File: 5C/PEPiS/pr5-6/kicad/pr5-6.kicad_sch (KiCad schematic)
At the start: 10 parts, among them U1 STM32F103C8T6

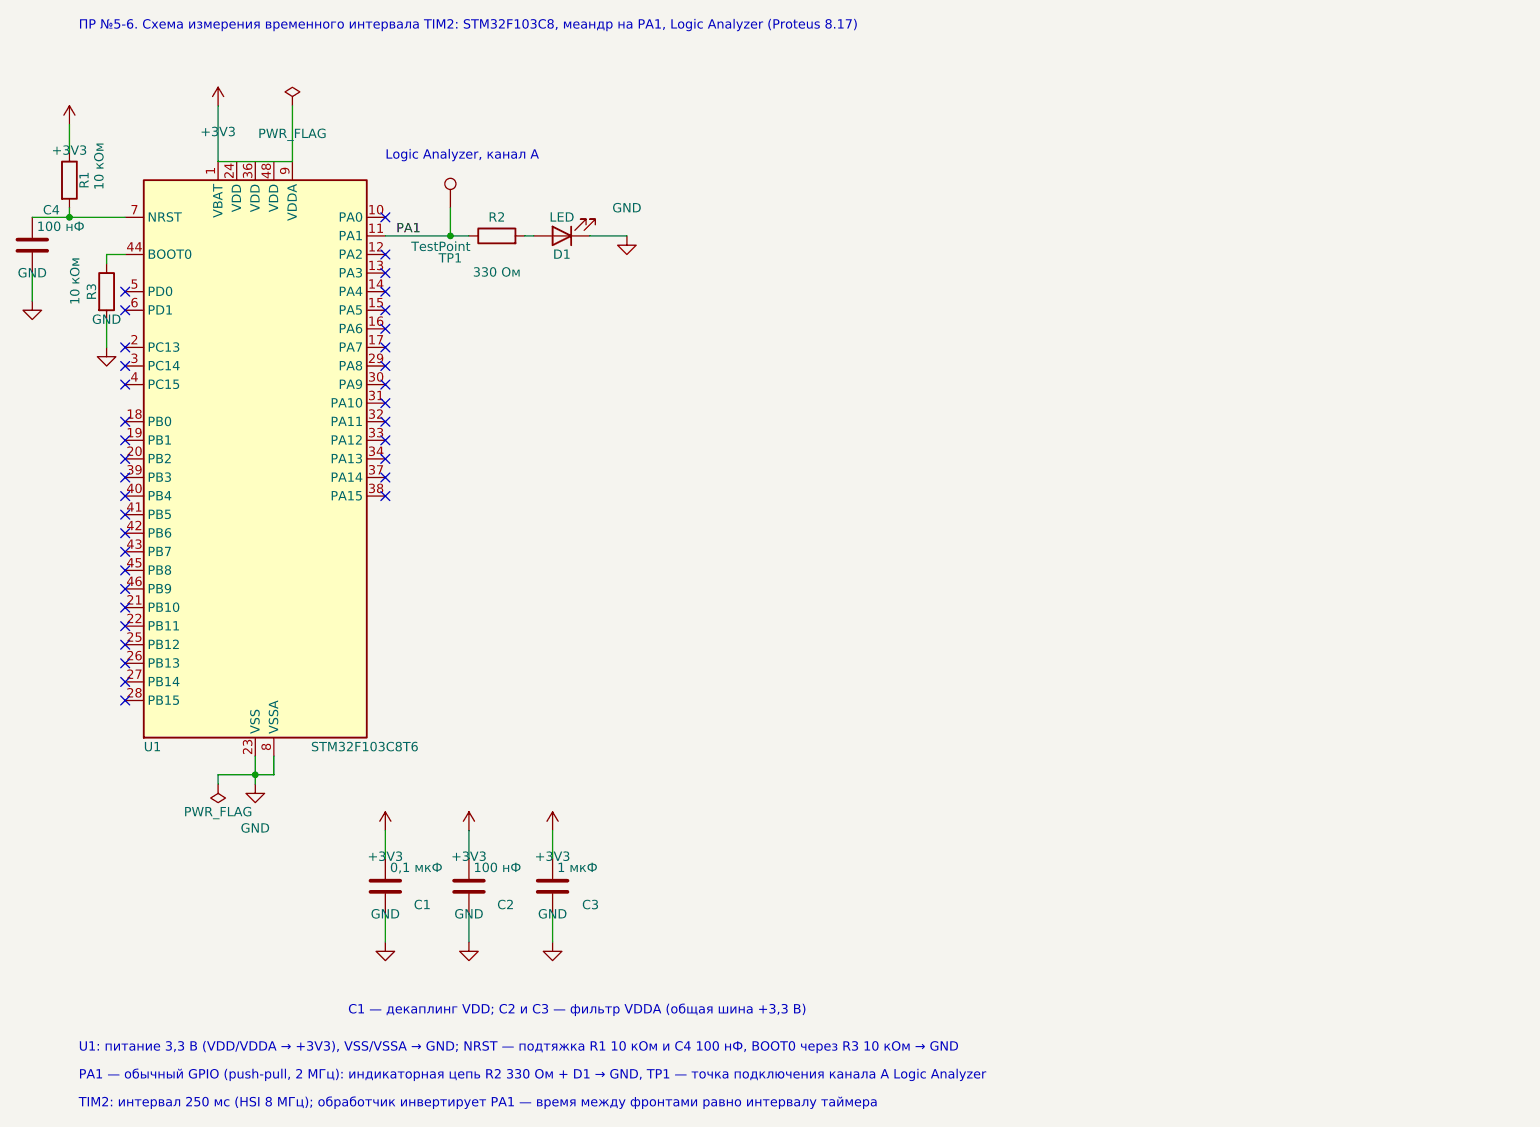
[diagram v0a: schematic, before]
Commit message: style(pr5-6): canonical schematic cleanup, docs sources and lesson
Title No to #, TestPoint value hidden, power/flag refs hidden,
duplicate floating text removed, whole sheet re-placed (ERC 0/0).
Add TZ/listing sources, PLAN and cleanup lesson.
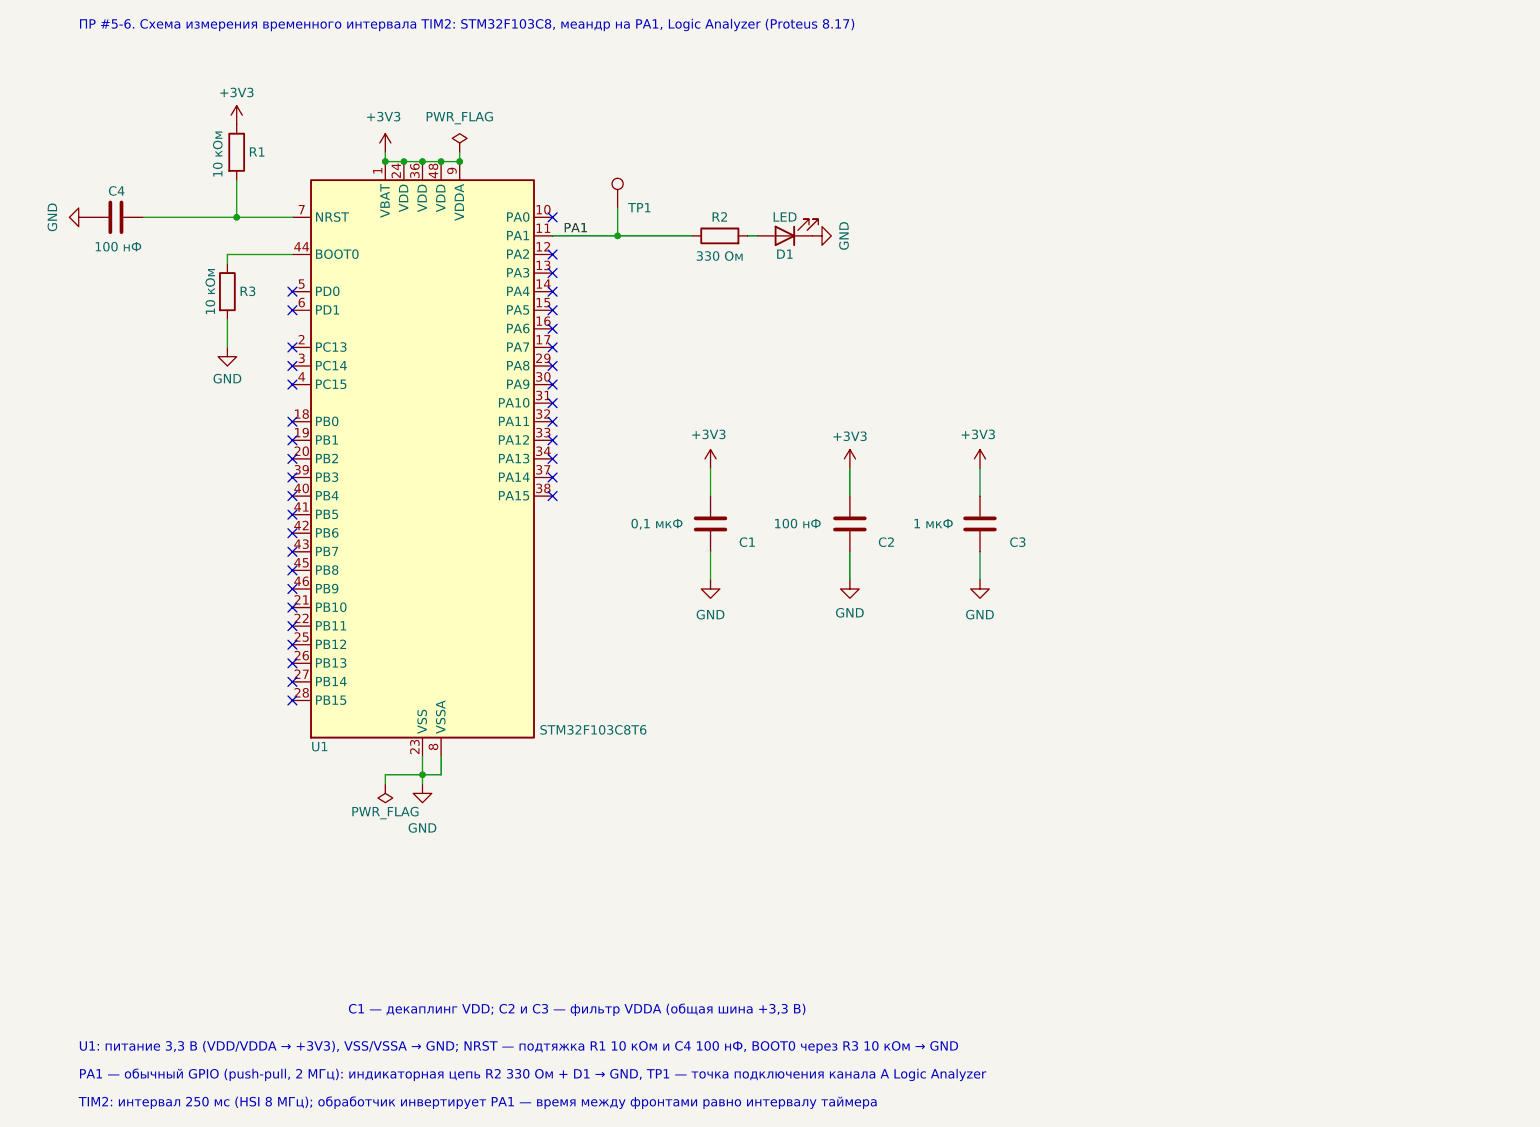
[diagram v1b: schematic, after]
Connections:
- net GND: now also C4.1; no longer C4.2
- net at R1.2, U1.7 (NRST): now also C4.2; no longer C4.1
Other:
- note added: "ПР #5-6. Схема измерения временного интервала TIM2: STM32F103C8, меандр на PA1, Logic Analyzer (Proteus 8.17)"
- note removed: "Logic Analyzer, канал A"
- note removed: "ПР №5-6. Схема измерения временного интервала TIM2: STM32F103C8, меандр на PA1, Logic Analyzer (Proteus 8.17)"
- title: ПР №5-6. Измерение временного интервала TIM2 (STM32F103C8, меандр на PA1) -> ПР #5-6. Изм. временного интервала TIM2 (меандр на PA1)
- moved on the sheet: C1, C2, C3, C4, D1, R1, R2, R3, TP1, U1
